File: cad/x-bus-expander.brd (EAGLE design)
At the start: 100 x 50 mm, 56 parts, among them IC1 MCP23017SO, IC2 MCP23017SO

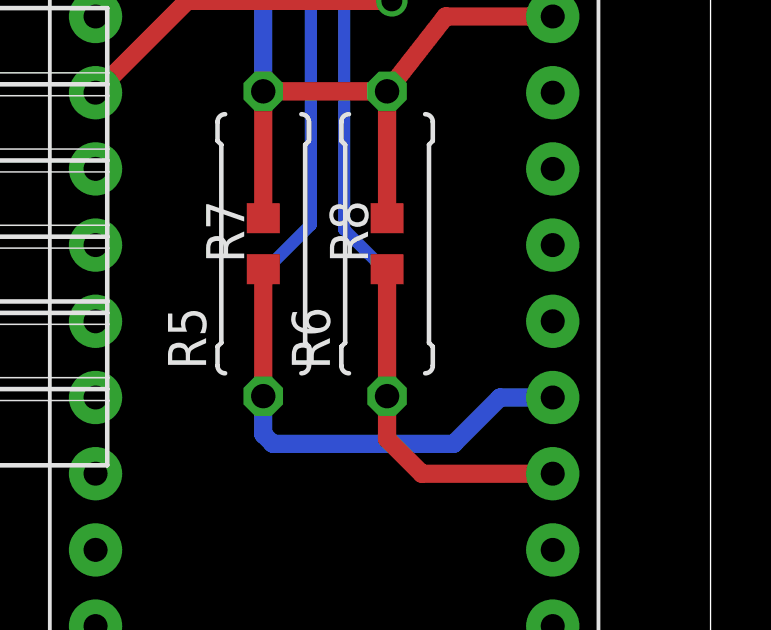
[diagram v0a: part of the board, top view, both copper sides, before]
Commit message: Fixed a pcb bug when Arduion nano v2/v3 have different I2C pins placement.
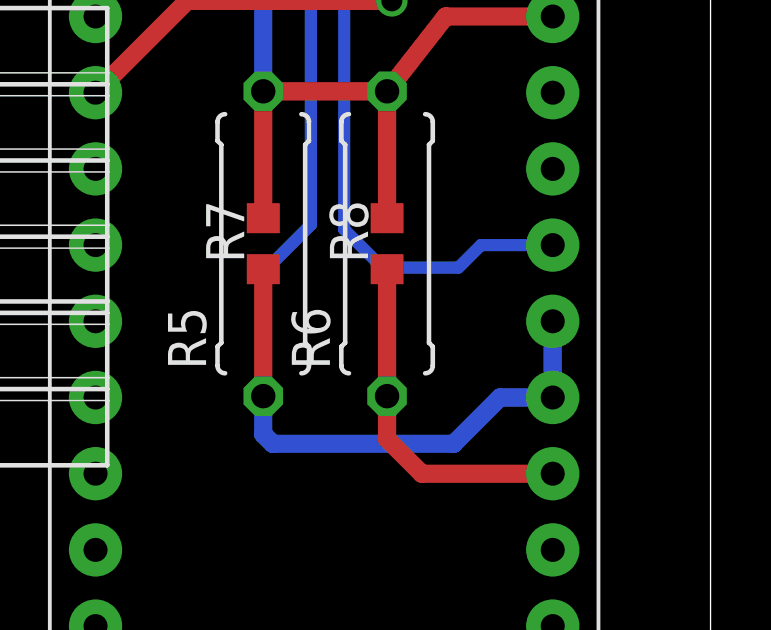
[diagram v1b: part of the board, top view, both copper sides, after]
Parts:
- R1: value (none) -> 10k
- RN1, RN2: value (none) -> 8x1k
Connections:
- net NANO_SCL: now also U$1.A2
- net NANO_SDA: now also U$1.A3
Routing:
- net NANO_SCL: track 38.9 -> 44.9 mm
- net NANO_SDA: track 43.5 -> 46.0 mm
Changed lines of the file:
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@@
 <attribute name="VALUE" x="15.73" y="39.92" size="1.778" layer="27" ratio="10" rot="R180"/>
 </element>
-<element name="RN1" library="resistor-sil" package="SIL9" value="" x="17" y="34.655" smashed="yes">
+<element name="RN1" library="resistor-sil" package="SIL9" value="8x1k" x="17" y="34.655" smashed="yes">
 <attribute name="OC_NEWARK" value="unknown" x="17" y="34.655" size="1.778" layer="27" display="off"/>
 <attribute name="MPN" value="" x="17" y="34.655" size="1.778" layer="27" display="off"/>
@@
 <attribute name="VALUE" x="33.6075" y="19.06625" size="1.27" layer="27" rot="R90"/>
 </element>
-<element name="R1" library="rcl" package="R0603" value="" x="34.7825" y="32.27375" smashed="yes" rot="R90">
+<element name="R1" library="rcl" package="R0603" value="10k" x="34.7825" y="32.27375" smashed="yes" rot="R90">
 <attribute name="NAME" x="35.4175" y="33.86125" size="1.27" layer="25" rot="R90"/>
 <attribute name="VALUE" x="36.6875" y="31.63875" size="1.27" layer="27" rot="R90"/>
@@
 <attribute name="VALUE" x="55.73" y="39.92" size="1.778" layer="27" ratio="10" rot="R180"/>
 </element>
-<element name="RN2" library="resistor-sil" package="SIL9" value="" x="52.555" y="34.655" smashed="yes">
+<element name="RN2" library="resistor-sil" package="SIL9" value="8x1k" x="52.555" y="34.655" smashed="yes">
 <attribute name="OC_NEWARK" value="unknown" x="52.555" y="8.62" size="1.9304" layer="27" ratio="15" display="off"/>
 <attribute name="MPN" value="" x="52.555" y="8.62" size="1.9304" layer="27" ratio="15" display="off"/>
@@
 <contactref element="R7" pad="1"/>
 <wire x1="85.09" y1="23.915" x2="85.09" y2="19.685" width="0.6096" layer="1"/>
+<contactref element="U$1" pad="A3"/>
+<wire x1="94.74" y1="19.64" x2="94.74" y2="22.18" width="0.6096" layer="16"/>
 </signal>
 <signal name="NANO_SCL">
@@
 <contactref element="IO" pad="4"/>
 <contactref element="R6" pad="1"/>
-<wire x1="89.2175" y1="19.685" x2="89.2175" y2="23.8125" width="0.4064" layer="16"/>
-<wire x1="89.2175" y1="23.8125" x2="87.78875" y2="25.24125" width="0.4064" layer="16"/>
 <wire x1="87.78875" y1="25.24125" x2="87.78875" y2="41.275" width="0.4064" layer="16"/>
 <wire x1="87.78875" y1="41.275" x2="88.61125" y2="42.0975" width="0.4064" layer="16"/>
@@
 <contactref element="R8" pad="1"/>
 <wire x1="89.2175" y1="23.915" x2="89.2175" y2="19.685" width="0.6096" layer="1"/>
+<contactref element="U$1" pad="A2"/>
+<wire x1="94.74" y1="24.72" x2="92.3475" y2="24.72" width="0.4064" layer="16"/>
+<wire x1="92.3475" y1="24.72" x2="91.59875" y2="23.97125" width="0.4064" layer="16"/>
+<wire x1="89.05875" y1="23.97125" x2="87.78875" y2="25.24125" width="0.4064" layer="16"/>
+<wire x1="89.05875" y1="23.97125" x2="89.2175" y2="23.97125" width="0.4064" layer="16"/>
+<wire x1="89.2175" y1="23.97125" x2="89.2175" y2="23.915" width="0.4064" layer="16"/>
+<wire x1="89.2175" y1="23.915" x2="89.2175" y2="19.685" width="0.4064" layer="16"/>
+<wire x1="91.59875" y1="23.97125" x2="89.27375" y2="23.97125" width="0.4064" layer="16"/>
+<wire x1="89.27375" y1="23.97125" x2="89.2175" y2="23.915" width="0.4064" layer="16"/>
 </signal>
 <signal name="N$55">

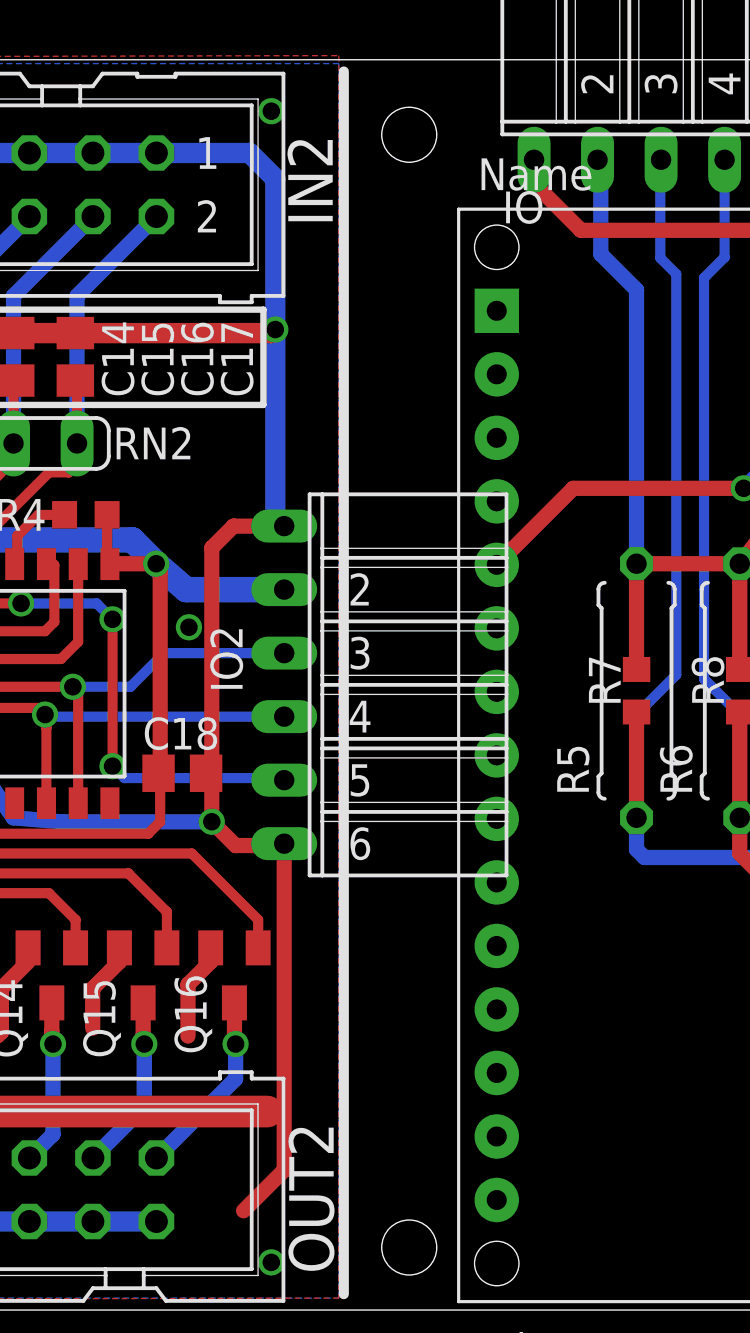
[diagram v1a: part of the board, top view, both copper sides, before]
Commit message: Updated schematic with some information and generated pdf for schematic.
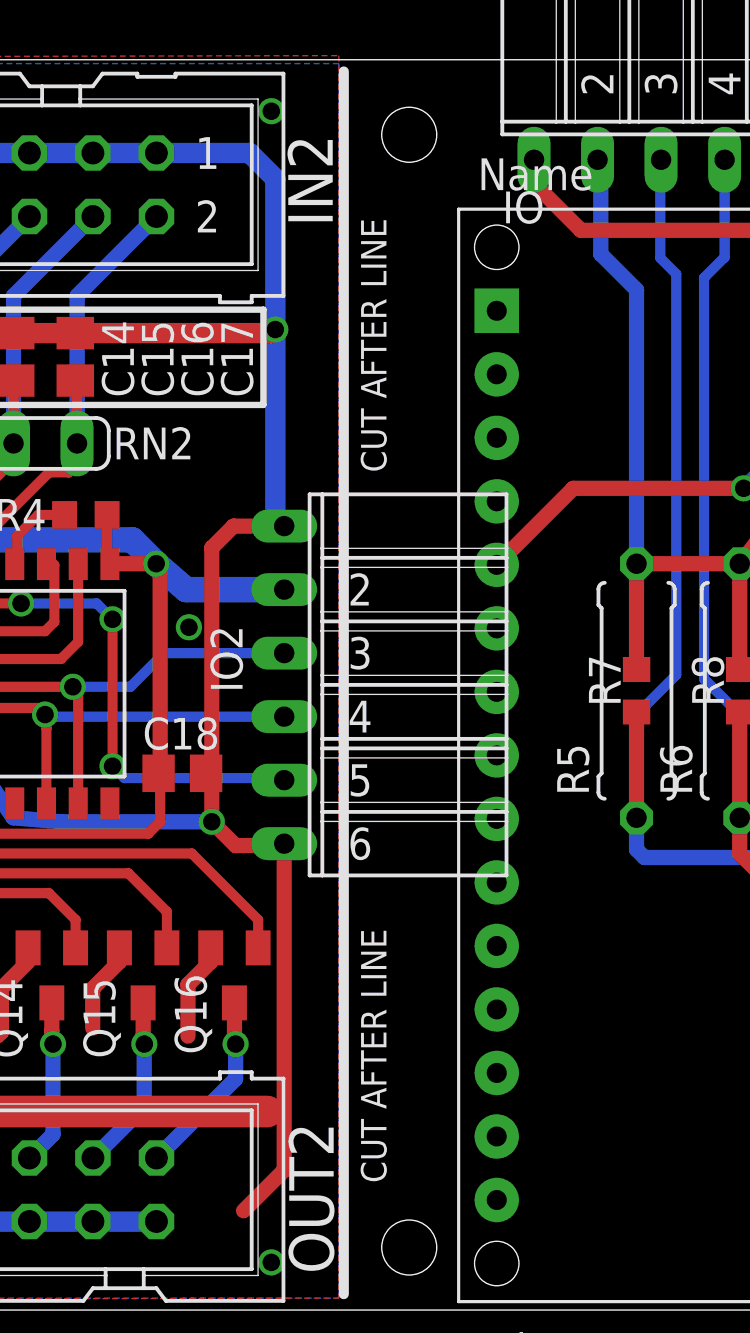
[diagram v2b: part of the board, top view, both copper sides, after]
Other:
- board text added: "CUT AFTER LINE"
